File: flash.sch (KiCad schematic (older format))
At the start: 3 parts, among them U1 AT25DF081A-SH

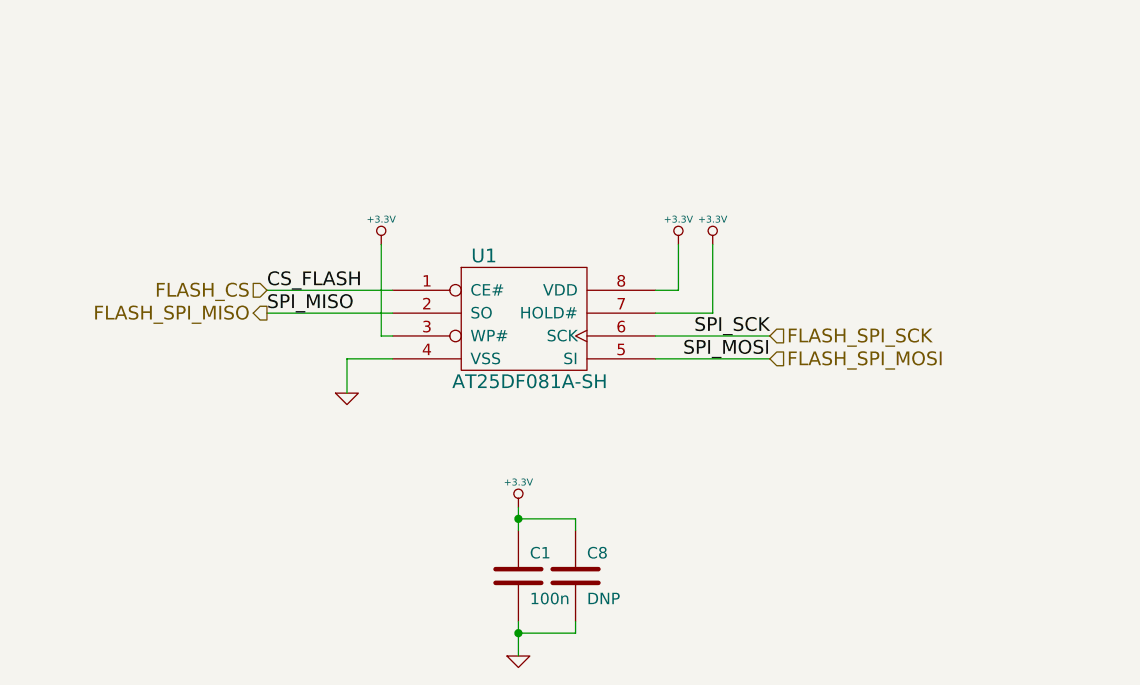
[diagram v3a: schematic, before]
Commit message: Changed to AT45 flash.
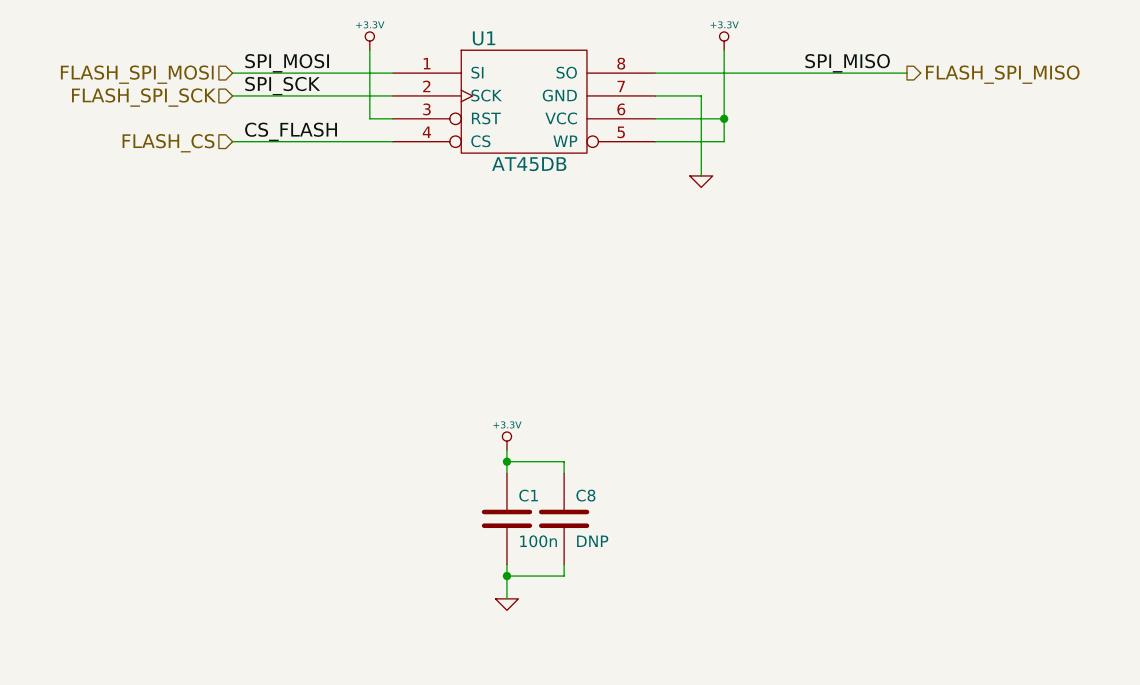
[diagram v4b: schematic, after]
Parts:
- removed U1: AT25DF081A-SH, symbol SPI-FLASH
- added U1: AT45DB, symbol AT45DB
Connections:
- net +3.3V: now also U1.3 (RST), U1.5 (WP), U1.6 (VCC)
- net FLASH_CS: now also U1.4 (CS)
- net FLASH_SPI_MISO: now also U1.8 (SO)
- net FLASH_SPI_MOSI: now also U1.1 (SI)
- net FLASH_SPI_SCK: now also U1.2 (SCK)
- net GND: now also U1.7 (GND)
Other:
- moved on the sheet: C1, C8
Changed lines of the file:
@@
-EESchema Schematic File Version 2  date Sat 08 Jun 2013 11:15:40 AM CEST
+EESchema Schematic File Version 2  date Sat 08 Jun 2013 06:16:56 PM CEST
 LIBS:power
 LIBS:device
@@
 $Descr A4 11700 8267
 encoding utf-8
-Sheet 2 10
+Sheet 3 10
 Title ""
 Date "8 jun 2013"
@@
 Comment4 ""
 $EndDescr
-Text HLabel 6700 3900 2    60   Input ~ 0
+Wire Wire Line
+	5050 2850 4950 2850
+Wire Wire Line
+	4950 2850 4950 2550
+Wire Wire Line
+	4350 2750 5050 2750
+Wire Wire Line
+	6200 2650 7300 2650
+Connection ~ 6500 2850
+Wire Wire Line
+	6500 2550 6500 2950
+Wire Wire Line
+	6500 2950 6200 2950
+Wire Wire Line
+	6500 2850 6200 2850
+Connection ~ 5550 4350
+Wire Wire Line
+	5550 4350 5800 4350
+Wire Wire Line
+	5800 4350 5800 4400
+Wire Wire Line
+	5550 4400 5550 4300
+Wire Wire Line
+	5550 4950 5550 4800
+Wire Wire Line
+	5800 4800 5800 4850
+Wire Wire Line
+	5800 4850 5550 4850
+Connection ~ 5550 4850
+Wire Wire Line
+	6200 2750 6400 2750
+Wire Wire Line
+	6400 2750 6400 3100
+Wire Wire Line
+	4350 2950 5050 2950
+Wire Wire Line
+	4350 2650 5050 2650
+$Comp
+L +3.3V #PWR?
+U 1 1 51B358E6
+P 4950 2550
+F 0 "#PWR?" H 4950 2510 30  0001 C CNN
+F 1 "+3.3V" H 4950 2660 30  0000 C CNN
+	1    4950 2550
+	1    0    0    -1
+$EndComp
+Text Label 4400 2650 0    60   ~ 0
+SPI_MOSI
+Text HLabel 4350 2650 0    60   Input ~ 0
 FLASH_SPI_MOSI
-Text HLabel 6700 3800 2    60   Input ~ 0
+Text Label 4400 2750 0    60   ~ 0
+SPI_SCK
+Text HLabel 4350 2750 0    60   Input ~ 0
 FLASH_SPI_SCK
-Text HLabel 4500 3700 0    60   Output ~ 0
+Text Label 4400 2950 0    60   ~ 0
+CS_FLASH
+Text HLabel 4350 2950 0    60   Input ~ 0
+FLASH_CS
+Text Label 6850 2650 0    60   ~ 0
+SPI_MISO
+Text HLabel 7300 2650 2    60   Output ~ 0
 FLASH_SPI_MISO
-Text HLabel 4500 3600 0    60   Input ~ 0
-FLASH_CS
+$Comp
+L GND #PWR?
+U 1 1 51B35829
+P 6400 3100
+F 0 "#PWR?" H 6400 3100 30  0001 C CNN
+F 1 "GND" H 6400 3030 30  0001 C CNN
+	1    6400 3100
+	1    0    0    -1
+$EndComp
+$Comp
+L +3.3V #PWR?
+U 1 1 51B35823
+P 6500 2550
+F 0 "#PWR?" H 6500 2510 30  0001 C CNN
+F 1 "+3.3V" H 6500 2660 30  0000 C CNN
+	1    6500 2550
+	1    0    0    -1
+$EndComp
+$Comp
+L AT45DB U1
+U 1 1 51B35808
+P 5650 2800
+F 0 "U1" H 5450 3100 60  0000 C CNN
+F 1 "AT45DB" H 5650 2550 60  0000 C CNN
+	1    5650 2800
+	1    0    0    -1
+$EndComp
 $Comp
 L C C1
 U 1 1 50CC832F
-P 5600 4850
-F 0 "C1" H 5650 4950 50  0000 L CNN
-F 1 "100n" H 5650 4750 50  0000 L CNN
-	1    5600 4850
-	1    0    0    -1
-$EndComp
-$Comp
-L SPI-FLASH U1
-U 1 1 50CC832E
-P 5650 3750
-F 0 "U1" H 5450 4050 60  0000 C CNN
-F 1 "AT25DF081A-SH" H 5650 3500 60  0000 C CNN
-	1    5650 3750
-	1    0    0    -1
-$EndComp
-Text Label 4500 3600 0    60   ~ 0
-CS_FLASH
-Text Label 4500 3700 0    60   ~ 0
-SPI_MISO
-Text Label 6700 3800 2    60   ~ 0
-SPI_SCK
-Text Label 6700 3900 2    60   ~ 0
-SPI_MOSI
-$Comp
-L GND #PWR015
-U 1 1 50CC832D
-P 4850 4050
-F 0 "#PWR015" H 4850 4050 30  0001 C CNN
-F 1 "GND" H 4850 3980 30  0001 C CNN
-	1    4850 4050
-	1    0    0    -1
-$EndComp
-$Comp
-L +3.3V #PWR016
-U 1 1 50CC832C
-P 6300 3400
-F 0 "#PWR016" H 6300 3360 30  0001 C CNN
-F 1 "+3.3V" H 6300 3510 30  0000 C CNN
-	1    6300 3400
-	1    0    0    -1
-$EndComp
-$Comp
-L +3.3V #PWR017
-U 1 1 50CC832B
-P 5000 3400
-F 0 "#PWR017" H 5000 3360 30  0001 C CNN
-F 1 "+3.3V" H 5000 3510 30  0000 C CNN
-	1    5000 3400
-	1    0    0    -1
-$EndComp
-$Comp
-L +3.3V #PWR018
-U 1 1 50CC832A
-P 6450 3400
-F 0 "#PWR018" H 6450 3360 30  0001 C CNN
-F 1 "+3.3V" H 6450 3510 30  0000 C CNN
-	1    6450 3400
+P 5550 4600
+F 0 "C1" H 5600 4700 50  0000 L CNN
+F 1 "100n" H 5600 4500 50  0000 L CNN
+	1    5550 4600
 	1    0    0    -1
 $EndComp
@@
 L +3.3V #PWR019
 U 1 1 50CC8329
-P 5600 4550
-F 0 "#PWR019" H 5600 4510 30  0001 C CNN
-F 1 "+3.3V" H 5600 4660 30  0000 C CNN
-	1    5600 4550
+P 5550 4300
+F 0 "#PWR019" H 5550 4260 30  0001 C CNN
+F 1 "+3.3V" H 5550 4410 30  0000 C CNN
+	1    5550 4300
 	1    0    0    -1
 $EndComp
@@
 L GND #PWR020
 U 1 1 50CC8328
-P 5600 5200
-F 0 "#PWR020" H 5600 5200 30  0001 C CNN
-F 1 "GND" H 5600 5130 30  0001 C CNN
-	1    5600 5200
+P 5550 4950
+F 0 "#PWR020" H 5550 4950 30  0001 C CNN
+F 1 "GND" H 5550 4880 30  0001 C CNN
+	1    5550 4950
 	1    0    0    -1
 $EndComp
@@
 L C C8
 U 1 1 50CC8327
-P 5850 4850
-F 0 "C8" H 5900 4950 50  0000 L CNN
-F 1 "DNP" H 5900 4750 50  0000 L CNN
-	1    5850 4850
+P 5800 4600
+F 0 "C8" H 5850 4700 50  0000 L CNN
+F 1 "DNP" H 5850 4500 50  0000 L CNN
+	1    5800 4600
 	1    0    0    -1
 $EndComp
-Connection ~ 5600 5100
-Wire Wire Line
-	5600 5100 5850 5100
-Wire Wire Line
-	5850 5100 5850 5050
-Wire Wire Line
-	5600 5200 5600 5050
-Wire Wire Line
-	6300 3400 6300 3600
-Wire Wire Line
-	4850 4050 4850 3900
-Wire Wire Line
-	4850 3900 5050 3900
-Wire Wire Line
-	5050 3700 4500 3700
-Wire Wire Line
-	5050 3600 4500 3600
-Wire Wire Line
-	6300 3600 6200 3600
-Wire Wire Line
-	6200 3800 6700 3800
-Wire Wire Line
-	6200 3900 6700 3900
-Wire Wire Line
-	5050 3800 5000 3800
-Wire Wire Line
-	5000 3800 5000 3400
-Wire Wire Line
-	6200 3700 6450 3700
-Wire Wire Line
-	6450 3700 6450 3400
-Wire Wire Line
-	5600 4650 5600 4550
-Wire Wire Line
-	5850 4650 5850 4600
-Wire Wire Line
-	5850 4600 5600 4600
-Connection ~ 5600 4600
 $EndSCHEMATC
